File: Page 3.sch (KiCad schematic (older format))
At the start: 2 parts

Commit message: Updates
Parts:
- added C309: 22uF, symbol Device:CP1
- added LS301: Piezo Buzzer, Name Plate Class Project:Buzzer_TDK_PS1240P02BT_D12.2mm_H6.5mm, symbol Device:Buzzer
- R302: footprint (none) -> Resistor_SMD:R_0603_1608Metric_Pad1.05x0.95mm_HandSolder
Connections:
- net GND: now also LS301.2 (+)
- new net: C309.2, LS301.1 (-)
- new net BUZZER: C309.1
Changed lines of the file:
@@
 $Descr A4 11693 8268
 encoding utf-8
-Sheet 4 4
+Sheet 4 10
 Title ""
 Date ""
@@
 F 0 "R302" V 2650 5950 50  0000 L BNN
 F 1 "470k" V 2750 5950 50  0000 L BNN
-F 2 "" V 2780 6050 50  0001 C CNN
+F 2 "Resistor_SMD:R_0603_1608Metric_Pad1.05x0.95mm_HandSolder" V 2780 6050 50  0001 C CNN
 F 3 "~" H 2850 6050 50  0001 C CNN
 	1    2850 6050
@@
 AR Path="/5EAC05C2/5ECEB251" Ref="#PWR?"  Part="1"
 AR Path="/5EACA483/5ECEB251" Ref="#PWR?"  Part="1"
-F 0 "#PWR?" H 3150 5900 50  0001 C CNN
+AR Path="/5ECEA271/5ECEB251" Ref="#PWR0105"  Part="1"
+F 0 "#PWR0105" H 3150 5900 50  0001 C CNN
 F 1 "GND" H 3155 5977 50  0000 C CNN
 F 2 "" H 3150 6150 50  0001 C CNN
@@
 Text GLabel 1850 6050 0    50   Input ~ 0
 LED_IND
+$Comp
+L Device:Buzzer BUZZ?
+U 1 1 5ECECE8C
+P 9050 5300
+AR Path="/5EACA483/5ECECE8C" Ref="BUZZ?"  Part="1"
+AR Path="/5ECE9FD3/5ECECE8C" Ref="BUZZ?"  Part="1"
+AR Path="/5ECEA271/5ECECE8C" Ref="LS301"  Part="1"
+F 0 "LS301" H 9200 5350 50  0000 L CNN
+F 1 "Piezo Buzzer" H 9200 5250 50  0000 L CNN
+F 2 "Name Plate Class Project:Buzzer_TDK_PS1240P02BT_D12.2mm_H6.5mm" V 9025 5400 50  0001 C CNN
+F 3 "http://www.puiaudio.com/pdf/AST-03008MR-R.pdf" V 9025 5400 50  0001 C CNN
+	1    9050 5300
+	1    0    0    -1
+$EndComp
+Wire Wire Line
+	8950 5400 8800 5400
+Wire Wire Line
+	8800 5400 8800 5550
+$Comp
+L power:GND #PWR?
+U 1 1 5ECECE94
+P 8800 5550
+AR Path="/5EACA483/5ECECE94" Ref="#PWR?"  Part="1"
+AR Path="/5ECE9FD3/5ECECE94" Ref="#PWR?"  Part="1"
+AR Path="/5ECEA271/5ECECE94" Ref="#PWR0108"  Part="1"
+F 0 "#PWR0108" H 8800 5300 50  0001 C CNN
+F 1 "GND" H 8805 5377 50  0000 C CNN
+F 2 "" H 8800 5550 50  0001 C CNN
+F 3 "" H 8800 5550 50  0001 C CNN
+	1    8800 5550
+	1    0    0    -1
+$EndComp
+$Comp
+L Device:CP1 C?
+U 1 1 5ECECE9A
+P 8650 5200
+AR Path="/5EACA483/5ECECE9A" Ref="C?"  Part="1"
+AR Path="/5ECE9FD3/5ECECE9A" Ref="C?"  Part="1"
+AR Path="/5ECEA271/5ECECE9A" Ref="C309"  Part="1"
+F 0 "C309" V 8902 5200 50  0000 C CNN
+F 1 "22uF" V 8811 5200 50  0000 C CNN
+F 2 "" H 8650 5200 50  0001 C CNN
+F 3 "~" H 8650 5200 50  0001 C CNN
+	1    8650 5200
+	0    -1   -1   0
+$EndComp
+Text GLabel 8300 5200 0    50   Input ~ 0
+BUZZER
+Wire Wire Line
+	8800 5200 8950 5200
+Wire Wire Line
+	8500 5200 8300 5200
 $EndSCHEMATC

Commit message: Updates
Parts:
- C309: value 22uF -> 2.2uF; footprint (none) -> Name Plate Class Project:CAP_430X430N; DigiKey Part No. (none) -> PCE4295CT-ND; Field4 (none) -> Panasonic EEE-1VA2R2NR; Mftr Part No. (none) -> Panasonic EEE-1VA2R2NR
- D305: footprint (none) -> Name Plate Class Project:LED_G-GX; DigiKey Part No. (none) -> 754-1580-6-ND; Mftr Part No. (none) -> Kingbright APA3010CGCK-GX
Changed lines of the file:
@@
 F 0 "D305" H 2350 5800 50  0000 R TNN
 F 1 "BLUE LED" H 2350 5900 50  0000 R TNN
-F 2 "" H 2300 6050 50  0001 C CNN
-F 3 "~" H 2300 6050 50  0001 C CNN
+F 2 "Name Plate Class Project:LED_G-GX" H 2300 6050 50  0001 C CNN
+F 3 "http://www.kingbrightusa.com/images/catalog/SPEC/APA3010CGCK-GX.pdf" H 2300 6050 50  0001 C CNN
+F 4 "754-1580-6-ND" H 2300 6050 50  0001 C CNN "DigiKey Part No."
+F 5 "Kingbright APA3010CGCK-GX" H 2300 6050 50  0001 C CNN "Mftr Part No."
 	1    2300 6050
 	-1   0    0    1
@@
 AR Path="/5ECEA271/5ECECE9A" Ref="C309"  Part="1"
 F 0 "C309" V 8902 5200 50  0000 C CNN
-F 1 "22uF" V 8811 5200 50  0000 C CNN
-F 2 "" H 8650 5200 50  0001 C CNN
-F 3 "~" H 8650 5200 50  0001 C CNN
+F 1 "2.2uF" V 8811 5200 50  0000 C CNN
+F 2 "Name Plate Class Project:CAP_430X430N" H 8650 5200 50  0001 C CNN
+F 3 "https://media.digikey.com/pdf/Data%20Sheets/Panasonic%20Electronic%20Components/S_Series,Type_V_Rev2018.pdf" H 8650 5200 50  0001 C CNN
+F 4 "Panasonic EEE-1VA2R2NR" H 8650 5200 50  0001 C CNN "Field4"
+F 5 "PCE4295CT-ND" H 8650 5200 50  0001 C CNN "DigiKey Part No."
+F 6 "Panasonic EEE-1VA2R2NR" H 8650 5200 50  0001 C CNN "Mftr Part No."
+F 7 "" H 8650 5200 50  0001 C CNN "URL"
 	1    8650 5200
 	0    -1   -1   0

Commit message: Updates
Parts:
- added C301: 10uF, Capacitor_SMD:C_0805_2012Metric_Pad1.15x1.40mm_HandSolder, symbol Device:C
- added C305, C306, C307, C308: 0.1uF, Capacitor_SMD:C_0603_1608Metric_Pad1.05x0.95mm_HandSolder, symbol Device:C
- added D301, D302, D303, D304: WS2812B, LED_SMD:LED_WS2812B_PLCC4_5.0x5.0mm_P3.2mm, symbol LED:WS2812B
- added R301: R22K0, Resistor_SMD:R_0603_1608Metric_Pad1.05x0.95mm_HandSolder, symbol Device:R
- added TP301: TP_ADDR_LED, Connector_Wire:SolderWirePad_1x01_SMD_5x10mm, symbol Connector:TestPoint
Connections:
- net GND: now also C301.2, C305.2, C306.2, C307.2, C308.2, D301.3 (VSS), D302.3 (VSS), D303.3 (VSS), D304.3 (VSS)
- new net: D301.2 (DOUT), D302.4 (DIN)
- new net: D301.4 (DIN), R301.2
- new net: D302.2 (DOUT), D303.4 (DIN)
- new net: D303.2 (DOUT), D304.4 (DIN)
- new net +5V: C301.1, C305.1, C306.1, C307.1, C308.1, D301.1 (VDD), D302.1 (VDD), D303.1 (VDD), D304.1 (VDD)
- new net ADDR_LED: R301.1, TP301.1
- no-connect marks 0 -> 1
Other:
- moved on the sheet: C309, D305, LS301, R302

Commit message: Updates
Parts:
- C305, C306, C307, C308: Mftr Part No. (none) -> Yageo CC0603KPX7R7BB104
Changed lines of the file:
@@
 F 2 "Capacitor_SMD:C_0603_1608Metric_Pad1.05x0.95mm_HandSolder" H 4438 3100 50  0001 C CNN
 F 3 "https://www.yageo.com/upload/media/product/productsearch/datasheet/mlcc/UPY-GPHC_X7R_6.3V-to-50V_18.pdf" H 4400 3250 50  0001 C CNN
+F 4 "Yageo CC0603KPX7R7BB104" H 4400 3250 50  0001 C CNN "Mftr Part No."
 	1    4400 3250
 	1    0    0    -1
@@
 F 2 "Capacitor_SMD:C_0603_1608Metric_Pad1.05x0.95mm_HandSolder" H 5588 3100 50  0001 C CNN
 F 3 "https://www.yageo.com/upload/media/product/productsearch/datasheet/mlcc/UPY-GPHC_X7R_6.3V-to-50V_18.pdf" H 5550 3250 50  0001 C CNN
+F 4 "Yageo CC0603KPX7R7BB104" H 5550 3250 50  0001 C CNN "Mftr Part No."
 	1    5550 3250
 	1    0    0    -1
@@
 F 2 "Capacitor_SMD:C_0603_1608Metric_Pad1.05x0.95mm_HandSolder" H 6738 3100 50  0001 C CNN
 F 3 "https://www.yageo.com/upload/media/product/productsearch/datasheet/mlcc/UPY-GPHC_X7R_6.3V-to-50V_18.pdf" H 6700 3250 50  0001 C CNN
+F 4 "Yageo CC0603KPX7R7BB104" H 6700 3250 50  0001 C CNN "Mftr Part No."
 	1    6700 3250
 	1    0    0    -1
@@
 F 2 "Capacitor_SMD:C_0603_1608Metric_Pad1.05x0.95mm_HandSolder" H 7888 3100 50  0001 C CNN
 F 3 "https://www.yageo.com/upload/media/product/productsearch/datasheet/mlcc/UPY-GPHC_X7R_6.3V-to-50V_18.pdf" H 7850 3250 50  0001 C CNN
+F 4 "Yageo CC0603KPX7R7BB104" H 7850 3250 50  0001 C CNN "Mftr Part No."
 	1    7850 3250
 	1    0    0    -1
@@
 Wire Wire Line
 	5050 3550 5550 3550
-Connection ~ 5550 3550
-Wire Wire Line
-	5550 3550 6050 3550
-Connection ~ 6200 3550
 Wire Wire Line
 	6200 3550 6700 3550
@@
 Wire Wire Line
 	3900 2250 5050 2250
-Connection ~ 3900 2250
-Wire Wire Line
-	3900 2250 3900 2100
+Wire Wire Line
+	8350 2250 8350 2100
 Connection ~ 7850 3550
 NoConn ~ 7650 2950
@@
 L power:+5V #PWR0101
 U 1 1 5EB43851
-P 3900 2100
-F 0 "#PWR0101" H 3900 1950 50  0001 C CNN
-F 1 "+5V" H 3915 2273 50  0000 C CNN
-F 2 "" H 3900 2100 50  0001 C CNN
-F 3 "" H 3900 2100 50  0001 C CNN
-	1    3900 2100
+P 8350 2100
+F 0 "#PWR0101" H 8350 1950 50  0001 C CNN
+F 1 "+5V" H 8365 2273 50  0000 C CNN
+F 2 "" H 8350 2100 50  0001 C CNN
+F 3 "" H 8350 2100 50  0001 C CNN
+	1    8350 2100
 	1    0    0    -1
 $EndComp
@@
 L power:GND #PWR0102
 U 1 1 5EB44FF3
-P 6050 3550
-F 0 "#PWR0102" H 6050 3300 50  0001 C CNN
-F 1 "GND" H 6055 3377 50  0000 C CNN
-F 2 "" H 6050 3550 50  0001 C CNN
-F 3 "" H 6050 3550 50  0001 C CNN
-	1    6050 3550
-	1    0    0    -1
-$EndComp
-Connection ~ 6050 3550
-Wire Wire Line
-	6050 3550 6200 3550
+P 8350 3750
+F 0 "#PWR0102" H 8350 3500 50  0001 C CNN
+F 1 "GND" H 8355 3577 50  0000 C CNN
+F 2 "" H 8350 3750 50  0001 C CNN
+F 3 "" H 8350 3750 50  0001 C CNN
+	1    8350 3750
+	1    0    0    -1
+$EndComp
 Wire Wire Line
 	8350 3550 7850 3550
@@
 	1    0    0    -1
 $EndComp
+Connection ~ 8350 2250
+Connection ~ 6200 3550
+Connection ~ 5550 3550
+Wire Wire Line
+	5550 3550 6200 3550
+Wire Wire Line
+	8350 3550 8350 3750
+Connection ~ 8350 3550
 $EndSCHEMATC

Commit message: Updates
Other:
- note added: "2812 LEDs"
- note added: "Buzzer"
- note added: "Indicator LED"
- moved on the sheet: C301, C305, C306, C307, C308, C309, D301, D302, D303, D304, D305, LS301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

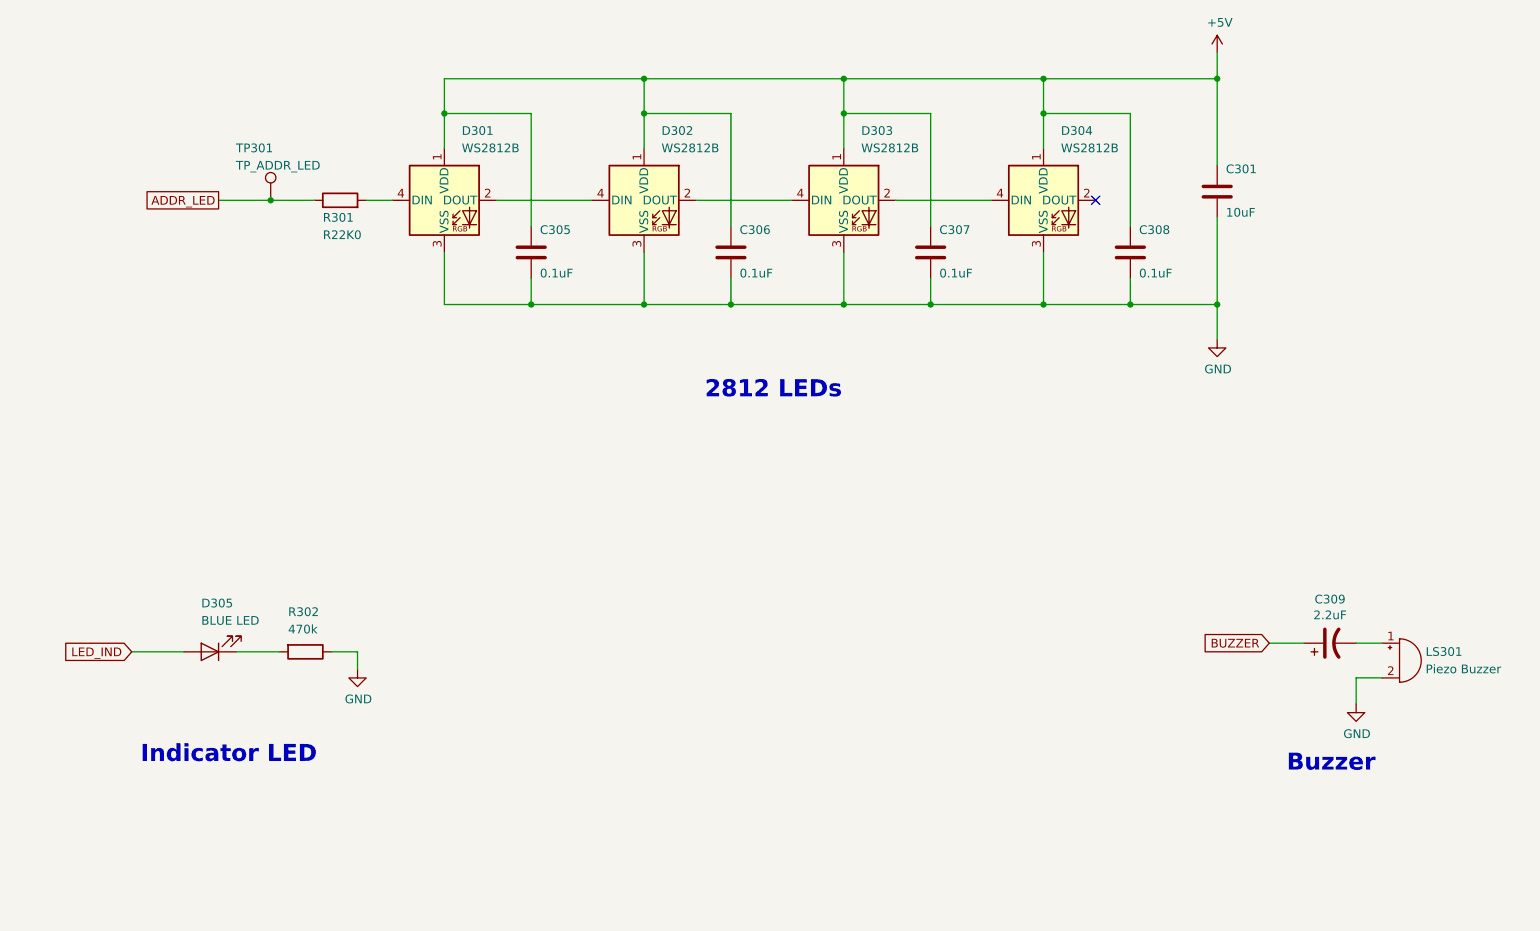
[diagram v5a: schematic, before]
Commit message: Switched to Hierarchical
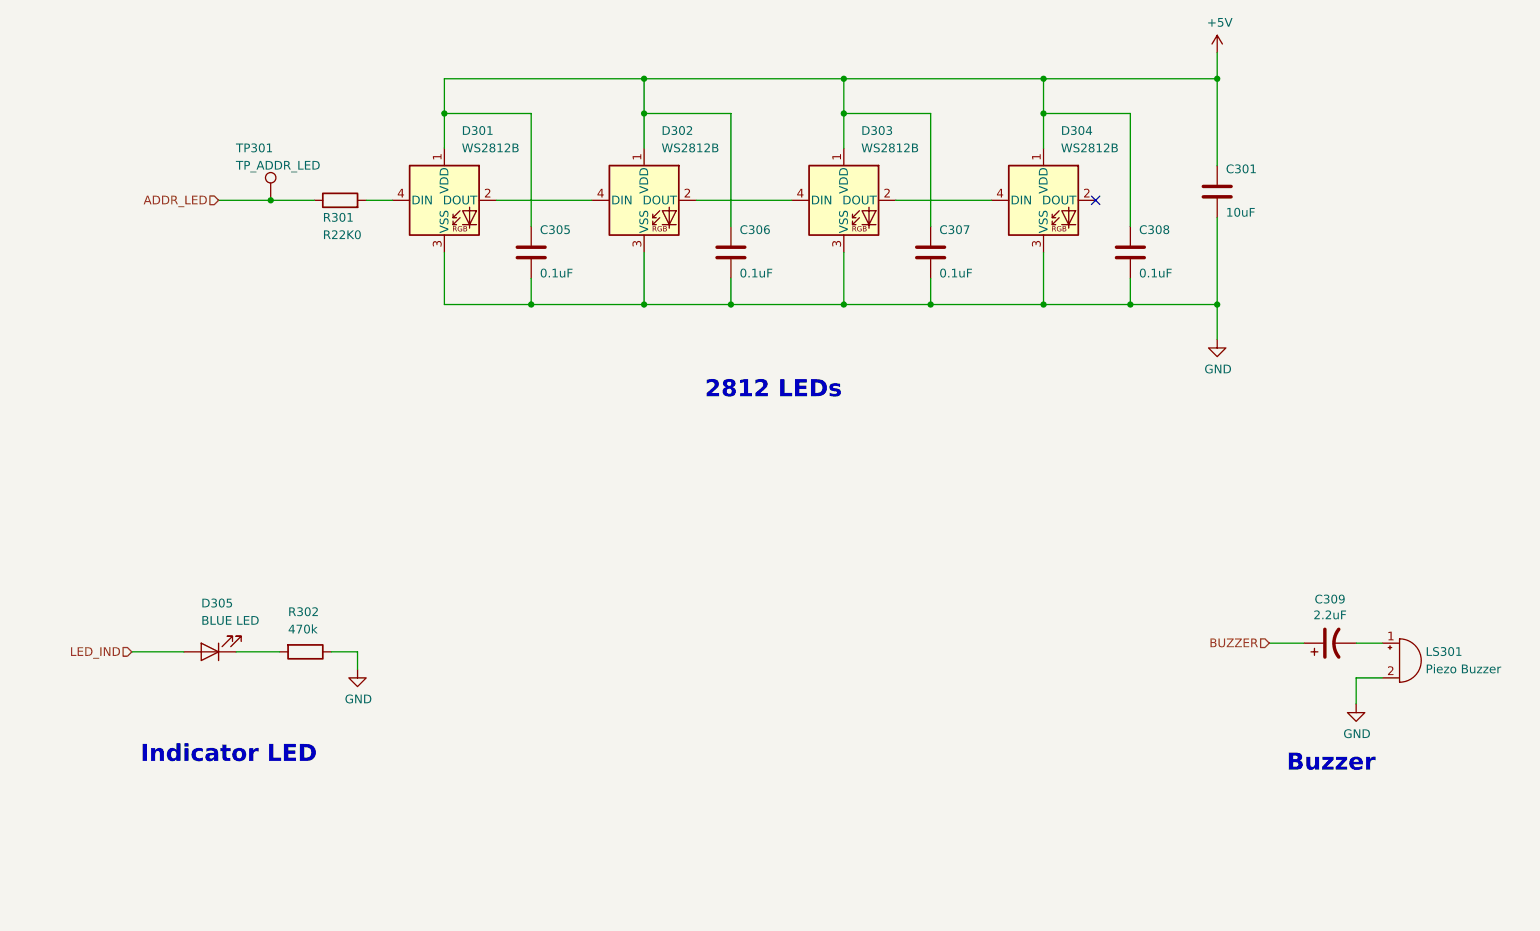
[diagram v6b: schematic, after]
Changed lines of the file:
@@
 Wire Wire Line
 	2350 4850 2050 4850
-Text GLabel 2050 4850 0    50   Input ~ 0
-LED_IND
 $Comp
 L Device:Buzzer LS?
@@
 	0    -1   -1   0
 $EndComp
-Text GLabel 8600 4800 0    50   Input ~ 0
-BUZZER
 Wire Wire Line
 	9100 4800 9250 4800
@@
 	2850 2250 2550 2250
 Connection ~ 2850 2250
-Text GLabel 2550 2250 0    50   UnSpc ~ 0
-ADDR_LED
 Wire Wire Line
 	3850 1950 3850 1750
@@
 Text Notes 8700 5550 0    98   ~ 20
 Buzzer
+Text HLabel 8600 4800 0    50   Input ~ 0
+BUZZER
+Text HLabel 2050 4850 0    50   Input ~ 0
+LED_IND
+Text HLabel 2550 2250 0    50   Input ~ 0
+ADDR_LED
 $EndSCHEMATC

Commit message: Updating to Final Revision
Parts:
- removed C301: 10uF, Capacitor_SMD:C_0805_2012Metric_Pad1.15x1.40mm_HandSolder, symbol Device:C
- added C302: 10uF, Name Plate Class Project:CAP_430X430N, symbol Device:CP1
- C301: renamed from C309; value 2.2uF -> 10uF
- renumbered C305 to C303, C306 to C304, C307 to C305, C308 to C306
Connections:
- net +5V: now also C302.1
- net GND: now also C302.2
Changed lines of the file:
@@
 $Descr A4 11693 8268
 encoding utf-8
-Sheet 4 10
+Sheet 4 9
 Title ""
 Date ""
@@
 AR Path="/5EACA483/5ECECE9A" Ref="C?"  Part="1"
 AR Path="/5ECE9FD3/5ECECE9A" Ref="C?"  Part="1"
-AR Path="/5ECEA271/5ECECE9A" Ref="C309"  Part="1"
-F 0 "C309" V 9202 4800 50  0000 C CNN
-F 1 "2.2uF" V 9111 4800 50  0000 C CNN
+AR Path="/5ECEA271/5ECECE9A" Ref="C301"  Part="1"
+F 0 "C301" V 9202 4800 50  0000 C CNN
+F 1 "10uF" V 9111 4800 50  0000 C CNN
 F 2 "Name Plate Class Project:CAP_430X430N" H 8950 4800 50  0001 C CNN
 F 3 "https://media.digikey.com/pdf/Data%20Sheets/Panasonic%20Electronic%20Components/S_Series,Type_V_Rev2018.pdf" H 8950 4800 50  0001 C CNN
@@
 AR Path="/5EAC05C2/5EB2D593" Ref="C?"  Part="1"
 AR Path="/5EACA483/5EB2D593" Ref="C?"  Part="1"
-AR Path="/5ECEA271/5EB2D593" Ref="C305"  Part="1"
-F 0 "C305" H 4400 2650 50  0000 L BNN
+AR Path="/5ECEA271/5EB2D593" Ref="C303"  Part="1"
+F 0 "C303" H 4400 2650 50  0000 L BNN
 F 1 "0.1uF" H 4400 2400 50  0000 L BNN
 F 2 "Capacitor_SMD:C_0603_1608Metric_Pad1.05x0.95mm_HandSolder" H 4388 2400 50  0001 C CNN
@@
 AR Path="/5EAC05C2/5EB315FC" Ref="C?"  Part="1"
 AR Path="/5EACA483/5EB315FC" Ref="C?"  Part="1"
-AR Path="/5ECEA271/5EB315FC" Ref="C306"  Part="1"
-F 0 "C306" H 5550 2650 50  0000 L BNN
+AR Path="/5ECEA271/5EB315FC" Ref="C304"  Part="1"
+F 0 "C304" H 5550 2650 50  0000 L BNN
 F 1 "0.1uF" H 5550 2400 50  0000 L BNN
 F 2 "Capacitor_SMD:C_0603_1608Metric_Pad1.05x0.95mm_HandSolder" H 5538 2400 50  0001 C CNN
@@
 AR Path="/5EAC05C2/5EB32756" Ref="C?"  Part="1"
 AR Path="/5EACA483/5EB32756" Ref="C?"  Part="1"
-AR Path="/5ECEA271/5EB32756" Ref="C307"  Part="1"
-F 0 "C307" H 6700 2650 50  0000 L BNN
+AR Path="/5ECEA271/5EB32756" Ref="C305"  Part="1"
+F 0 "C305" H 6700 2650 50  0000 L BNN
 F 1 "0.1uF" H 6700 2400 50  0000 L BNN
 F 2 "Capacitor_SMD:C_0603_1608Metric_Pad1.05x0.95mm_HandSolder" H 6688 2400 50  0001 C CNN
@@
 AR Path="/5EAC05C2/5EB3364B" Ref="C?"  Part="1"
 AR Path="/5EACA483/5EB3364B" Ref="C?"  Part="1"
-AR Path="/5ECEA271/5EB3364B" Ref="C308"  Part="1"
-F 0 "C308" H 7850 2650 50  0000 L BNN
+AR Path="/5ECEA271/5EB3364B" Ref="C306"  Part="1"
+F 0 "C306" H 7850 2650 50  0000 L BNN
 F 1 "0.1uF" H 7850 2400 50  0000 L BNN
 F 2 "Capacitor_SMD:C_0603_1608Metric_Pad1.05x0.95mm_HandSolder" H 7838 2400 50  0001 C CNN
@@
 Connection ~ 7800 2850
 NoConn ~ 7600 2250
-$Comp
-L Device:C C?
-U 1 1 5EB3F54E
-P 8300 2200
-AR Path="/5EB3F54E" Ref="C?"  Part="1"
-AR Path="/5EAC05C2/5EB3F54E" Ref="C?"  Part="1"
-AR Path="/5EACA483/5EB3F54E" Ref="C?"  Part="1"
-AR Path="/5ECEA271/5EB3F54E" Ref="C301"  Part="1"
-F 0 "C301" H 8350 2300 50  0000 L BNN
-F 1 "10uF" H 8350 2050 50  0000 L BNN
-F 2 "Capacitor_SMD:C_0805_2012Metric_Pad1.15x1.40mm_HandSolder" H 8338 2050 50  0001 C CNN
-F 3 "https://www.yageo.com/upload/media/product/productsearch/datasheet/mlcc/UPY-GPHC_X7R_6.3V-to-50V_18.pdf" H 8300 2200 50  0001 C CNN
-	1    8300 2200
-	1    0    0    -1
-$EndComp
 Wire Wire Line
 	8300 2350 8300 2850
@@
 Text HLabel 2550 2250 0    50   Input ~ 0
 ADDR_LED
+$Comp
+L Device:CP1 C?
+U 1 1 5ECD505A
+P 8300 2200
+AR Path="/5EACA483/5ECD505A" Ref="C?"  Part="1"
+AR Path="/5ECE9FD3/5ECD505A" Ref="C?"  Part="1"
+AR Path="/5ECEA271/5ECD505A" Ref="C302"  Part="1"
+F 0 "C302" H 8350 2300 50  0000 L CNN
+F 1 "10uF" H 8350 2050 50  0000 L CNN
+F 2 "Name Plate Class Project:CAP_430X430N" H 8300 2200 50  0001 C CNN
+F 3 "https://media.digikey.com/pdf/Data%20Sheets/Panasonic%20Electronic%20Components/S_Series,Type_V_Rev2018.pdf" H 8300 2200 50  0001 C CNN
+F 4 "Panasonic EEE-1VA2R2NR" H 8300 2200 50  0001 C CNN "Field4"
+F 5 "PCE4295CT-ND" H 8300 2200 50  0001 C CNN "DigiKey Part No."
+F 6 "Panasonic EEE-1VA2R2NR" H 8300 2200 50  0001 C CNN "Mftr Part No."
+F 7 "" H 8300 2200 50  0001 C CNN "URL"
+	1    8300 2200
+	1    0    0    -1
+$EndComp
 $EndSCHEMATC

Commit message: Updates
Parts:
- R301: value R22K0 -> 22K0; Manufacturer (none) -> TE Connectivity
- R302: Manufacturer (none) -> TE Connectivity
- TP301: value TP_ADDR_LED -> Test Point; Name (none) -> TP_ADDR_LED
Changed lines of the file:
@@
 F 2 "Resistor_SMD:R_0603_1608Metric_Pad1.05x0.95mm_HandSolder" V 2980 4850 50  0001 C CNN
 F 3 "~" H 3050 4850 50  0001 C CNN
+F 4 "TE Connectivity " H 3050 4850 50  0001 C CNN "Manufacturer"
 	1    3050 4850
 	0    1    1    0
@@
 AR Path="/5ECEA271/5EB2ABF4" Ref="R301"  Part="1"
 F 0 "R301" V 3150 2350 50  0000 R CNN
-F 1 "R22K0" V 3050 2350 50  0000 R CNN
+F 1 "22K0" V 3050 2350 50  0000 R CNN
 F 2 "Resistor_SMD:R_0603_1608Metric_Pad1.05x0.95mm_HandSolder" V 3180 2250 50  0001 C CNN
 F 3 "https://www.te.com/commerce/DocumentDelivery/DDEController?Action=srchrtrv&DocNm=1773204-3&DocType=DS&DocLang=English" H 3250 2250 50  0001 C CNN
+F 4 "TE Connectivity " H 3250 2250 50  0001 C CNN "Manufacturer"
 	1    3250 2250
 	0    -1   -1   0
@@
 AR Path="/5ECEA271/5EB2B88E" Ref="TP301"  Part="1"
 F 0 "TP301" H 2650 2550 50  0000 L CNN
-F 1 "TP_ADDR_LED" H 2650 2450 50  0000 L CNN
+F 1 "Test Point" H 2650 2450 50  0000 L CNN
 F 2 "Connector_Wire:SolderWirePad_1x01_SMD_5x10mm" H 3050 2250 50  0001 C CNN
-F 3 "~" H 3050 2250 50  0001 C CNN
+F 3 "None" H 3050 2250 50  0001 C CNN
+F 4 "TP_ADDR_LED" H 2850 2250 50  0001 C CNN "Name"
 	1    2850 2250
 	1    0    0    -1
